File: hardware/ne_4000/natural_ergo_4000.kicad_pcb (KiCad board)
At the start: 2 copper layers, 90 x 66 mm, 35 parts, among them J1 CONN_01X06, J2 CONN_02X03, J3 CONN_01X17, J4 CONN_01X17, J5 USB_OTGP, SW1 SW_Push, SW2 SW_Push, U1 ATMEGA88PA-AU, U2 74HC164, U3 74HC164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

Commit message: Replace shift registers with open drain version.
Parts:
- U2, U3, U4: value 74HC164 -> 6C595; footprint Housings_SOIC:SOIC-14_3.9x8.7mm_Pitch1.27mm -> Housings_SOIC:SOIC-16_3.9x9.9mm_Pitch1.27mm
- moved U3 24.4 mm to (101.8, 51.4), turned to 0 degrees
- moved U4 24.3 mm to (95.2, 74.4)
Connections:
- net Net-(D5-Pad1) renamed /USB-
- net Net-(D6-Pad1) renamed /USB+
- net Net-(R6-Pad2) renamed /USB+_M
- net Net-(R7-Pad2) renamed /USB-_M
- U1 pad 13: /SRCLR -> /SRD
- U1 pad 14: /SRD -> /SRCLR
- U2 pad 1: /SRD -> VCC
- U2 pad 10: /B6 -> /SRCLK
- U2 pad 11: /BX -> /B6
- U2 pad 12: /B9 -> Net-(U2-Pad12)
- U2 pad 13: /B1 -> Net-(U2-Pad13)
- U2 pad 14: VCC -> /B1
- U2 pad 7: GND -> /SRCLR
- U2 pad 8: /SRCLK -> GND
- U2 pad 9: /SRCLR -> /SER_23
- U3 pad 1: /B1 -> VCC
- U3 pad 10: /B10 -> /SRCLK
- U3 pad 11: /B11 -> /B16
- U3 pad 12: /B12 -> /B17
- U3 pad 13: /B13 -> /B18
- U3 pad 14: VCC -> /B8
- U3 pad 2: /B1 -> /SER_43
- U3 pad 3: /B22 -> /B12
- U3 pad 4: /B23 -> /B13
- U3 pad 5: Net-(U3-Pad5) -> /B14
- U3 pad 6: Net-(U3-Pad6) -> /B15
- U3 pad 7: GND -> /SRCLR
- U3 pad 8: /SRCLK -> GND
- U3 pad 9: /SRCLR -> Net-(U3-Pad9)
- U4 pad 1: /B13 -> VCC
- U4 pad 10: /B18 -> /SRCLK
- U4 pad 11: /B8 -> /B20
- U4 pad 12: /B20 -> /B7
- U4 pad 13: /B7 -> /B22
- U4 pad 14: VCC -> /B23
- U4 pad 2: /B13 -> /SER_23
- U4 pad 3: /B14 -> /BX
- U4 pad 4: /B15 -> /B9
- U4 pad 5: /B16 -> /B10
- U4 pad 6: /B17 -> /B11
- U4 pad 7: GND -> /SRCLR
- U4 pad 8: /SRCLK -> GND
- U4 pad 9: /SRCLR -> /SER_43
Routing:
- net /B1: track 135.0 -> 81.9 mm
- net /SER_23: track 0.00 -> 44.5 mm
- net /B9: track 87.4 -> 45.6 mm
- net /BX: track 118.9 -> 85.5 mm
- net /SER_43: track 0.00 -> 28.9 mm, vias 0 -> 2
- net /SRCLR: track 107.5 -> 133.3 mm
- net GND: track 253.7 -> 278.9 mm, vias 7 -> 9
- net /B7: track 57.1 -> 81.9 mm
- net /B20: track 22.3 -> 46.9 mm
- net /B13: track 45.6 -> 21.4 mm
- net /SRCLK: track 95.6 -> 115.4 mm
- net /B12: track 42.3 -> 23.9 mm
- net /B17: track 13.0 -> 22.2 mm
- net /B16: track 15.3 -> 21.2 mm
- net VCC: track 191.6 -> 197.2 mm
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
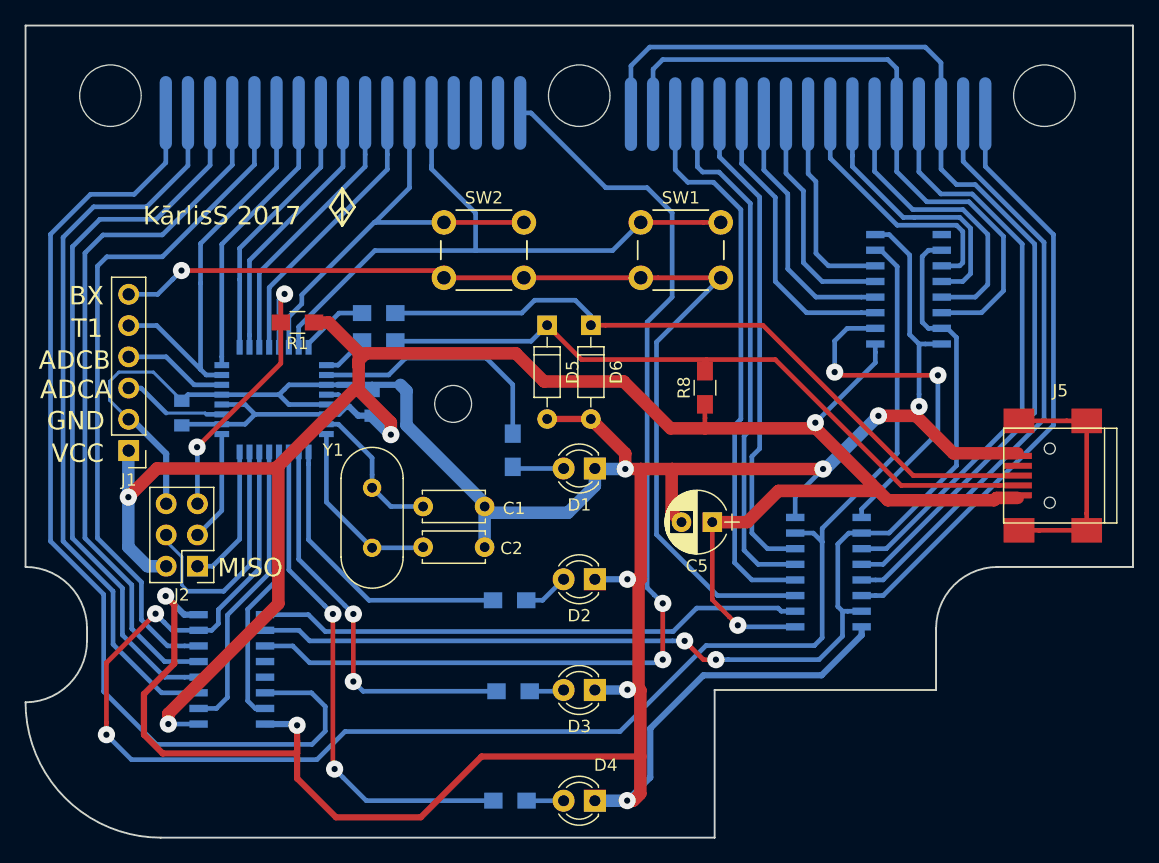
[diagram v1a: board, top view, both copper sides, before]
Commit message: Adjust PCB layout spacing
* increase spacing around middle screw
* move R8 to allow vertical cappacitor mounting
* add more labels
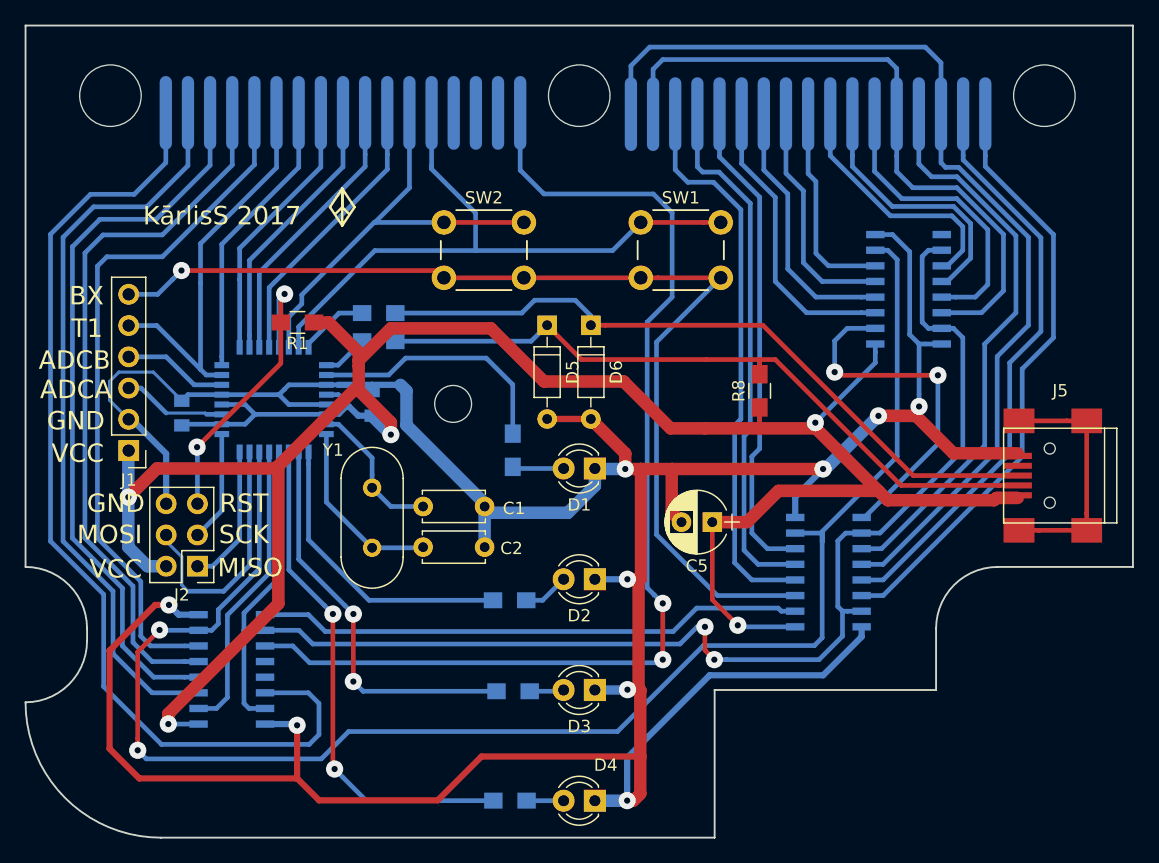
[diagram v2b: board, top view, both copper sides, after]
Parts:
- moved R8 4.45 mm to (89.7, 59.7)
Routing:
- net /SRCLR: track 133.3 -> 129.1 mm
- net /SRCLK: track 115.4 -> 119.0 mm
- net /B6: track 86.4 -> 89.1 mm
- net GND: track 278.9 -> 281.0 mm
- net VCC: track 197.2 -> 198.2 mm
- net /B1: track 81.9 -> 80.9 mm
- net /B20: track 46.9 -> 45.9 mm
- net /B5: track 55.6 -> 56.4 mm
- net /B7: track 81.9 -> 81.2 mm
- net /B4: track 57.3 -> 57.9 mm
- net /B3: track 58.5 -> 59.1 mm
- net /B17: track 22.2 -> 21.7 mm
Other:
- board text added: "MOSI"
- board text added: "RST"
- board text added: "SCK"
